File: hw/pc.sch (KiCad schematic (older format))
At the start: 8 parts, among them U601 74HC191, U602 74HC191, U603 74HC191, U604 74HC191, U605 74HC10, U606 74HC08, U607 74HC541, U608 74HC541

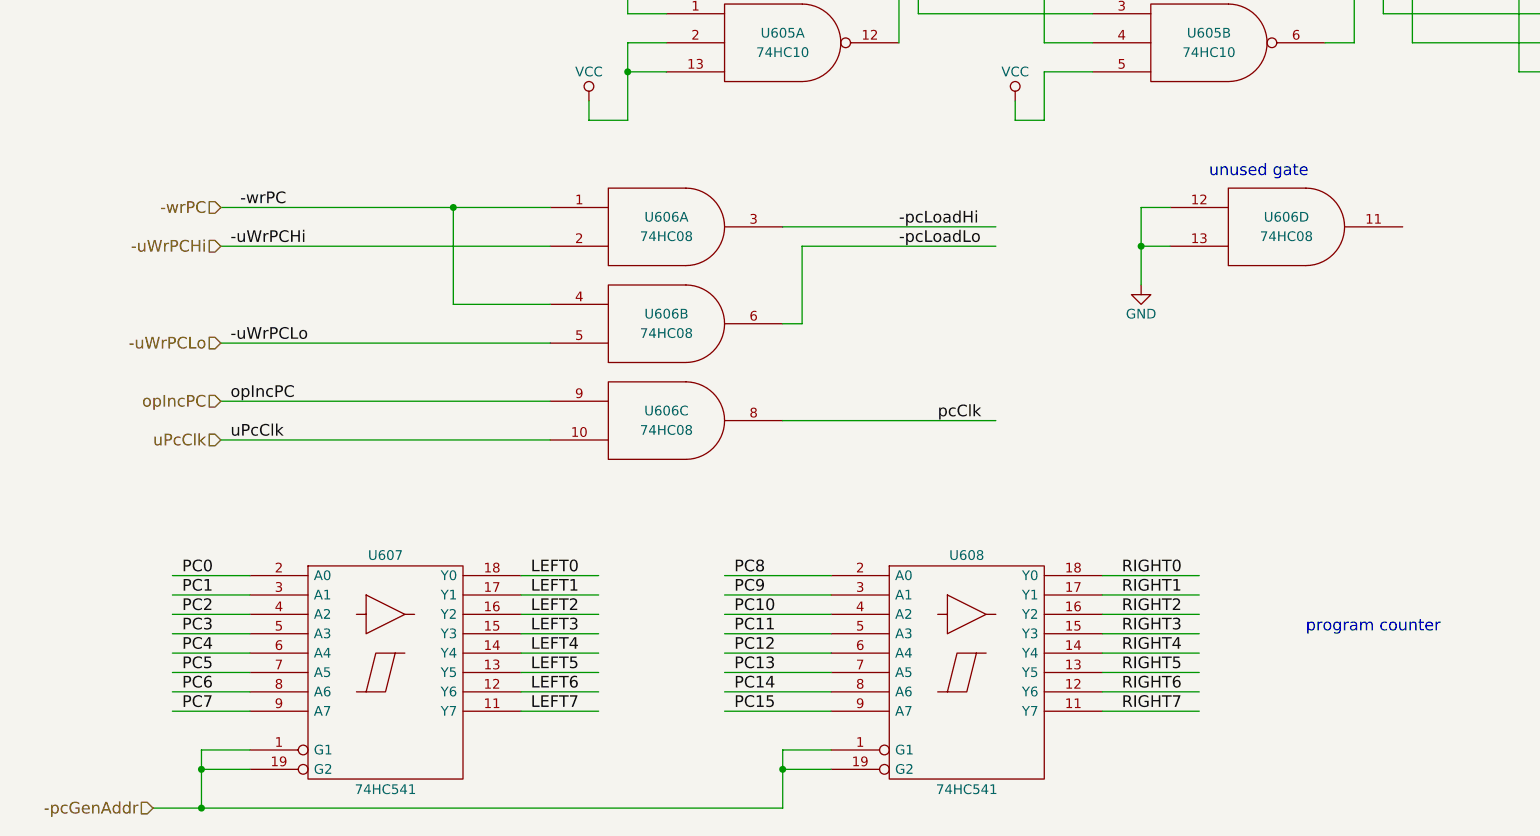
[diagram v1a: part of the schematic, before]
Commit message: use unused AND gate to allow 2 PC output enables
Both the opfetch logic and the microcode need to be
able to assert the contents of the PC onto the
left and right ALU input busses.
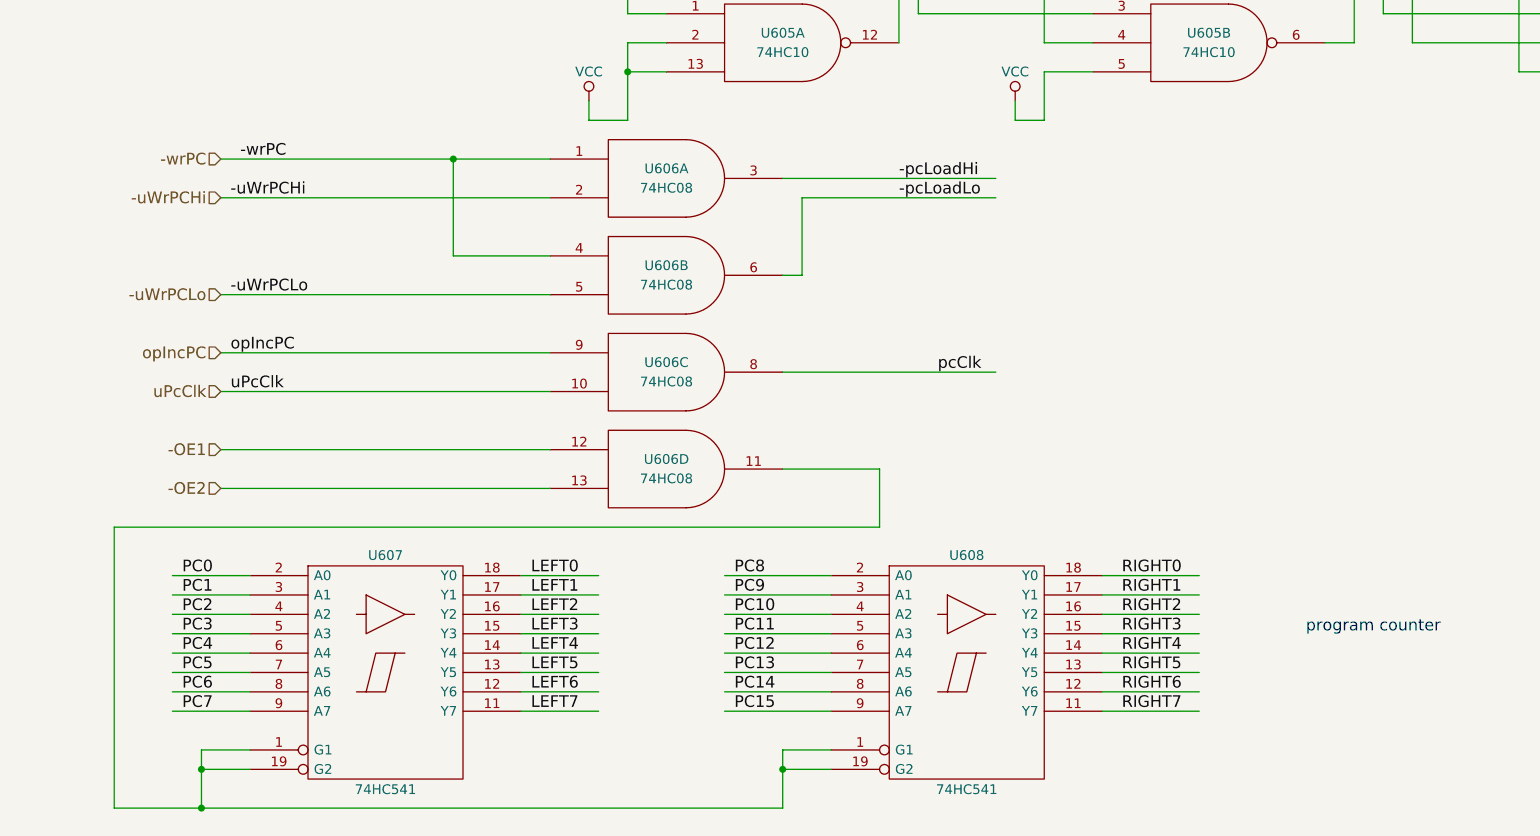
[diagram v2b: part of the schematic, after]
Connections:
- net labels added: -OE1, -OE2
- net labels removed: -pcGenAddr
- wire segments 184 -> 187
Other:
- note removed: "unused gate"
- moved on the sheet: U606A, U606B, U606C, U606D
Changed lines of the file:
@@
 Text Label 6200 7150 0    60   ~ 0
 RIGHT7
-Text HLabel 1200 7650 0    60   Input ~ 0
--pcGenAddr
+Text HLabel 1550 5800 0    60   Input ~ 0
+-OE1
 Text HLabel 1000 2050 0    60   Input ~ 0
 ALU0
@@
 Connection ~ 1450 7450
 Wire Wire Line
-	4450 7650 1200 7650
+	1000 7650 4450 7650
 Wire Wire Line
 	4700 7350 4450 7350
@@
 Connection ~ 6450 3150
 Wire Wire Line
-	1550 4550 3250 4550
-Text Label 1650 4550 0    60   ~ 0
+	1550 4300 3250 4300
+Text Label 1650 4300 0    60   ~ 0
 -wrPC
 Wire Wire Line
-	3250 5050 2750 5050
-Wire Wire Line
-	2750 5050 2750 4550
-Connection ~ 2750 4550
-Wire Wire Line
-	4450 4650 5550 4650
-Wire Wire Line
-	4450 5150 4550 5150
-Wire Wire Line
-	4550 5150 4550 4750
-Wire Wire Line
-	4550 4750 5550 4750
-Wire Wire Line
-	1550 5550 3250 5550
-Wire Wire Line
-	1550 5750 3250 5750
-Wire Wire Line
-	4450 5650 5550 5650
-Text Label 1600 5550 0    60   ~ 0
+	3250 4800 2750 4800
+Wire Wire Line
+	2750 4800 2750 4300
+Connection ~ 2750 4300
+Wire Wire Line
+	4450 4400 5550 4400
+Wire Wire Line
+	4450 4900 4550 4900
+Wire Wire Line
+	4550 4900 4550 4500
+Wire Wire Line
+	4550 4500 5550 4500
+Wire Wire Line
+	1550 5300 3250 5300
+Wire Wire Line
+	1550 5500 3250 5500
+Wire Wire Line
+	4450 5400 5550 5400
+Text Label 1600 5300 0    60   ~ 0
 opIncPC
 Wire Wire Line
-	3250 4750 1550 4750
-Wire Wire Line
-	3250 5250 1550 5250
-Text Label 1600 4750 0    60   ~ 0
+	3250 4500 1550 4500
+Wire Wire Line
+	3250 5000 1550 5000
+Text Label 1600 4500 0    60   ~ 0
 -uWrPCHi
-Text Label 1600 5250 0    60   ~ 0
+Text Label 1600 5000 0    60   ~ 0
 -uWrPCLo
-Text Label 1600 5750 0    60   ~ 0
+Text Label 1600 5500 0    60   ~ 0
 uPcClk
 Text Label 1450 700  0    60   ~ 0
@@
 Text Label 1450 1000 0    60   ~ 0
 -pcLoadLo
-Text HLabel 1550 4550 0    60   Input ~ 0
+Text HLabel 1550 4300 0    60   Input ~ 0
 -wrPC
-Text HLabel 1550 4750 0    60   Input ~ 0
+Text HLabel 1550 4500 0    60   Input ~ 0
 -uWrPCHi
-Text HLabel 1550 5250 0    60   Input ~ 0
+Text HLabel 1550 5000 0    60   Input ~ 0
 -uWrPCLo
-Text Label 5050 4650 0    60   ~ 0
+Text Label 5050 4400 0    60   ~ 0
 -pcLoadHi
-Text Label 5050 4750 0    60   ~ 0
+Text Label 5050 4500 0    60   ~ 0
 -pcLoadLo
 Text Label 1400 1500 0    60   ~ 0
 pcClk
-Text Label 5250 5650 0    60   ~ 0
+Text Label 5250 5400 0    60   ~ 0
 pcClk
-Text HLabel 1550 5550 0    60   Input ~ 0
+Text HLabel 1550 5300 0    60   Input ~ 0
 opIncPC
-Text HLabel 1550 5750 0    60   Input ~ 0
+Text HLabel 1550 5500 0    60   Input ~ 0
 uPcClk
 $Comp
 L 74LS08 U606
 U 1 1 5943D28D
-P 3850 4650
-F 0 "U606" H 3850 4700 50  0000 C CNN
-F 1 "74HC08" H 3850 4600 50  0000 C CNN
-F 2 "" H 3850 4650 50  0001 C CNN
-F 3 "" H 3850 4650 50  0001 C CNN
-	1    3850 4650
+P 3850 4400
+F 0 "U606" H 3850 4450 50  0000 C CNN
+F 1 "74HC08" H 3850 4350 50  0000 C CNN
+F 2 "" H 3850 4400 50  0001 C CNN
+F 3 "" H 3850 4400 50  0001 C CNN
+	1    3850 4400
 	1    0    0    -1
 $EndComp
@@
 L 74LS08 U606
 U 2 1 5943D2BC
-P 3850 5150
-F 0 "U606" H 3850 5200 50  0000 C CNN
-F 1 "74HC08" H 3850 5100 50  0000 C CNN
-F 2 "" H 3850 5150 50  0001 C CNN
-F 3 "" H 3850 5150 50  0001 C CNN
-	2    3850 5150
+P 3850 4900
+F 0 "U606" H 3850 4950 50  0000 C CNN
+F 1 "74HC08" H 3850 4850 50  0000 C CNN
+F 2 "" H 3850 4900 50  0001 C CNN
+F 3 "" H 3850 4900 50  0001 C CNN
+	2    3850 4900
 	1    0    0    -1
 $EndComp
@@
 L 74LS08 U606
 U 3 1 5943D307
-P 3850 5650
-F 0 "U606" H 3850 5700 50  0000 C CNN
-F 1 "74HC08" H 3850 5600 50  0000 C CNN
-F 2 "" H 3850 5650 50  0001 C CNN
-F 3 "" H 3850 5650 50  0001 C CNN
-	3    3850 5650
+P 3850 5400
+F 0 "U606" H 3850 5450 50  0000 C CNN
+F 1 "74HC08" H 3850 5350 50  0000 C CNN
+F 2 "" H 3850 5400 50  0001 C CNN
+F 3 "" H 3850 5400 50  0001 C CNN
+	3    3850 5400
 	1    0    0    -1
 $EndComp
@@
 L 74LS08 U606
 U 4 1 5943D865
-P 7050 4650
-F 0 "U606" H 7050 4700 50  0000 C CNN
-F 1 "74HC08" H 7050 4600 50  0000 C CNN
-F 2 "" H 7050 4650 50  0001 C CNN
-F 3 "" H 7050 4650 50  0001 C CNN
-	4    7050 4650
-	1    0    0    -1
-$EndComp
-Wire Wire Line
-	6450 4550 6300 4550
-Wire Wire Line
-	6300 4550 6300 4950
-Wire Wire Line
-	6450 4750 6300 4750
-Connection ~ 6300 4750
-$Comp
-L GND #PWR?
-U 1 1 5943DB03
-P 6300 4950
-F 0 "#PWR?" H 6300 4700 50  0001 C CNN
-F 1 "GND" H 6300 4800 50  0000 C CNN
-F 2 "" H 6300 4950 50  0001 C CNN
-F 3 "" H 6300 4950 50  0001 C CNN
-	1    6300 4950
-	1    0    0    -1
-$EndComp
-Text Notes 6650 4400 0    60   ~ 0
-unused gate
+P 3850 5900
+F 0 "U606" H 3850 5950 50  0000 C CNN
+F 1 "74HC08" H 3850 5850 50  0000 C CNN
+F 2 "" H 3850 5900 50  0001 C CNN
+F 3 "" H 3850 5900 50  0001 C CNN
+	4    3850 5900
+	1    0    0    -1
+$EndComp
+Wire Wire Line
+	3250 5800 1550 5800
+Wire Wire Line
+	3250 6000 1550 6000
+Text HLabel 1550 6000 0    60   Input ~ 0
+-OE2
+Wire Wire Line
+	4450 5900 4950 5900
+Wire Wire Line
+	4950 5900 4950 6200
+Wire Wire Line
+	4950 6200 1000 6200
+Wire Wire Line
+	1000 6200 1000 7650
 $EndSCHEMATC

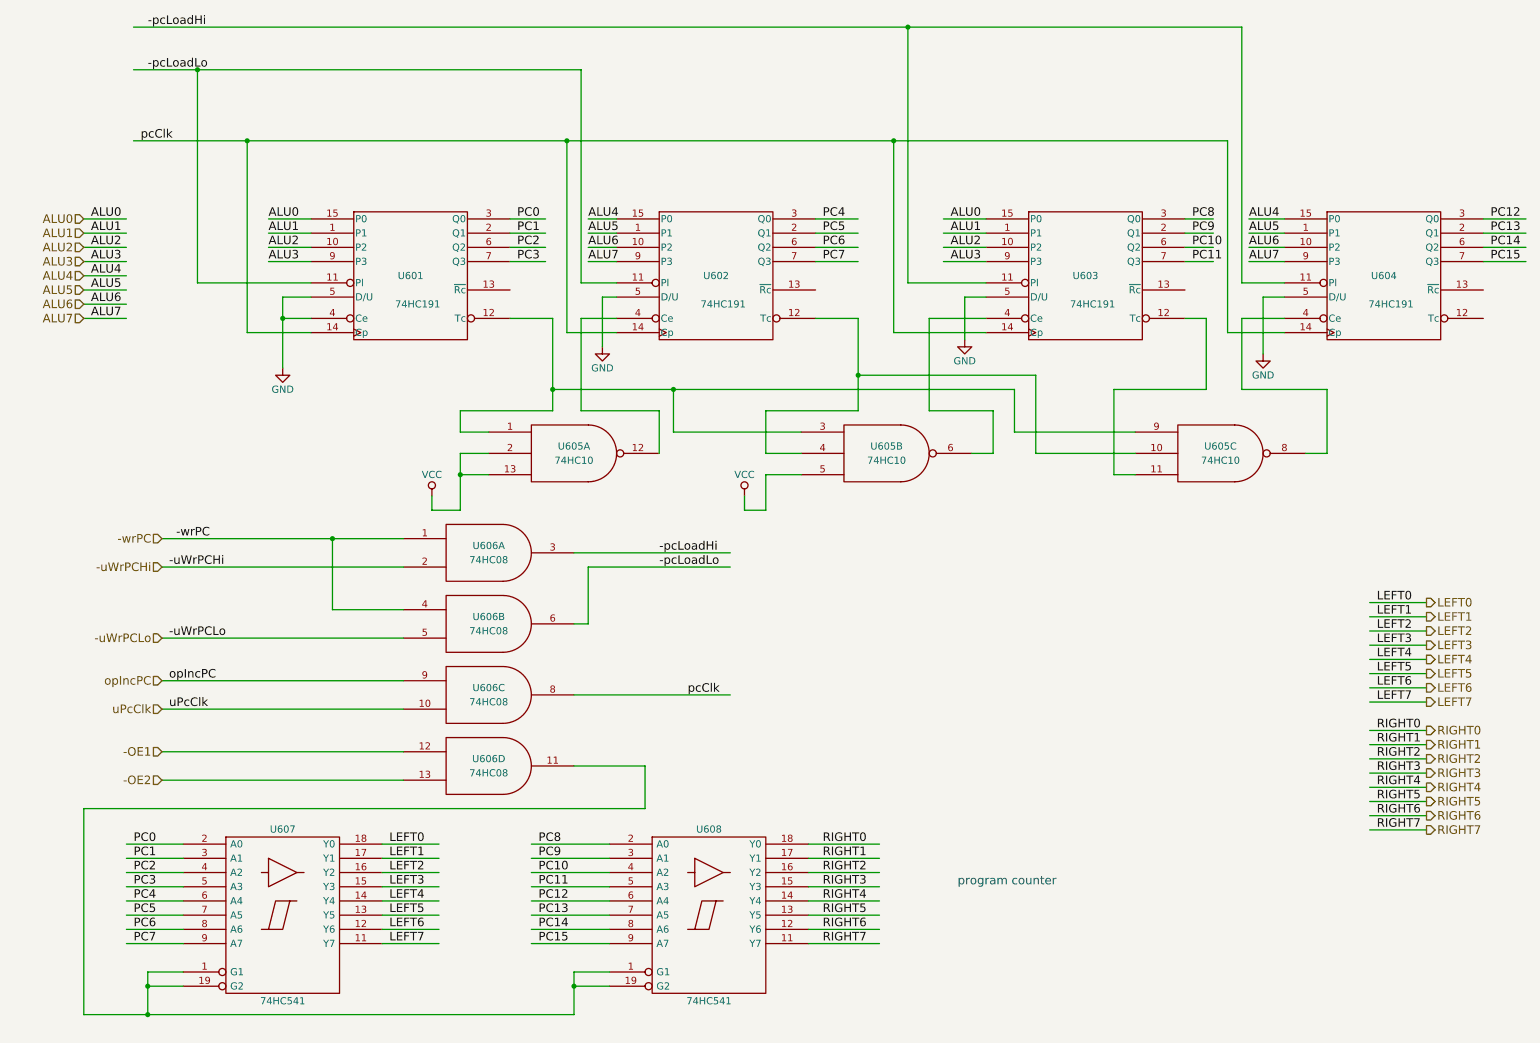
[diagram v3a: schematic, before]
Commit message: simplified control of output to left/right busses
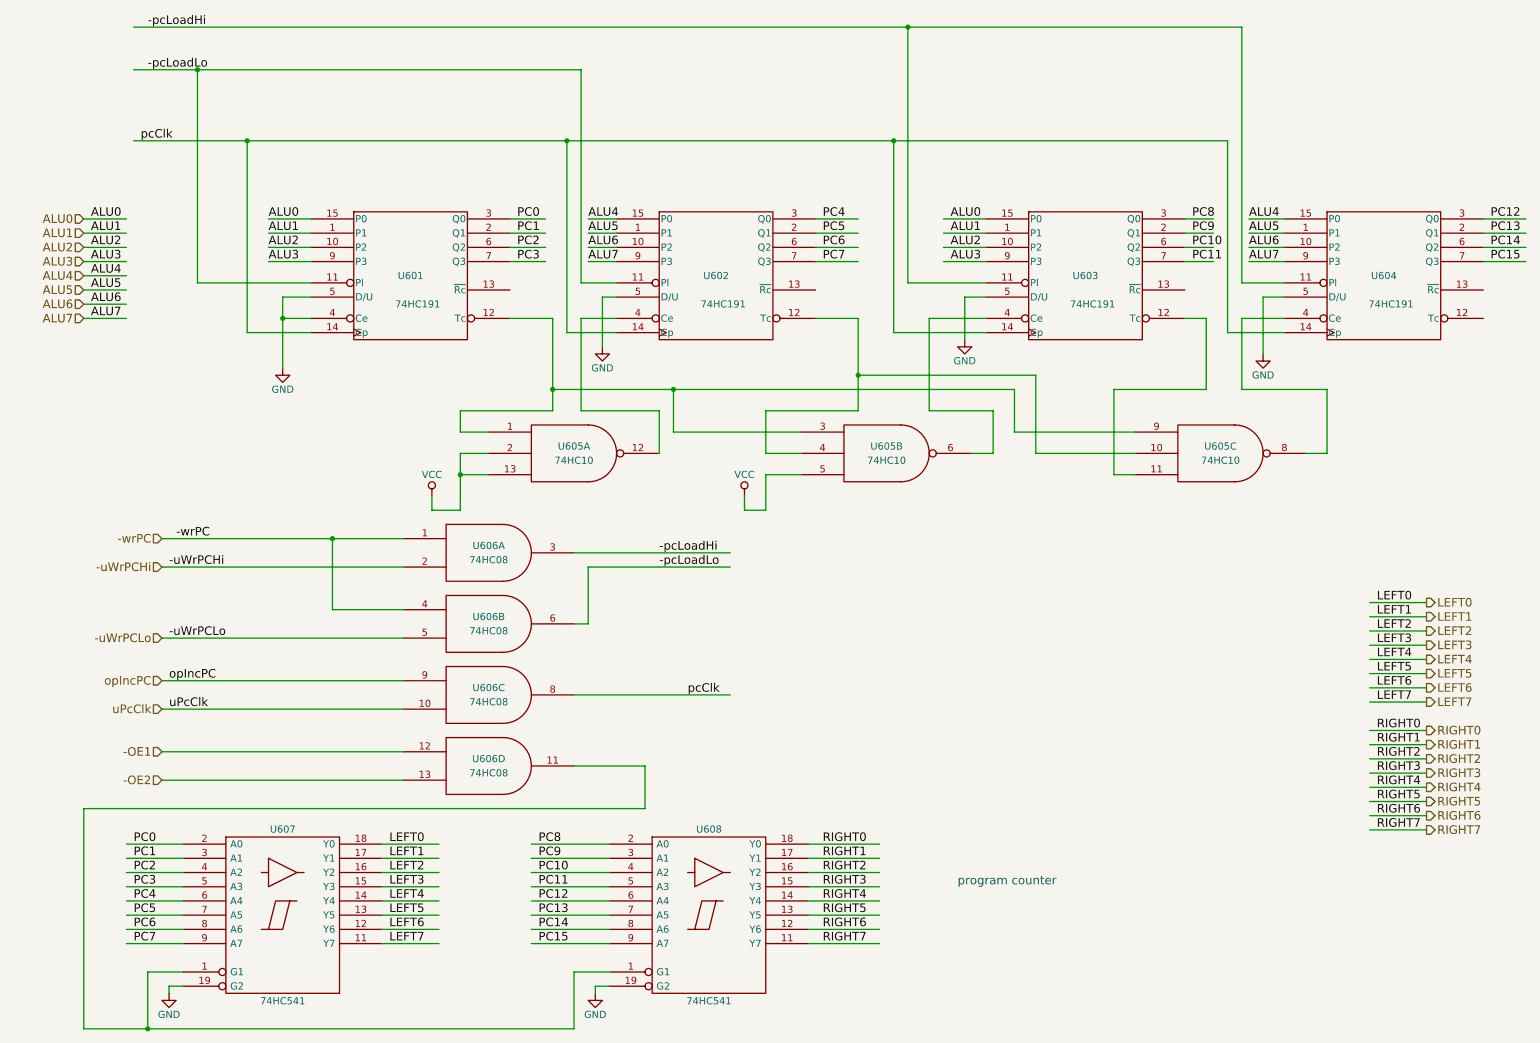
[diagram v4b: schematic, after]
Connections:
- wire segments 187 -> 201
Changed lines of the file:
@@
 	2600 2600 2400 2600
 Wire Wire Line
-	2400 2600 2400 3100
+	2400 2600 2400 2750
+Wire Wire Line
+	2400 2750 2400 3100
 Wire Wire Line
 	4750 2600 4650 2600
@@
 	9050 2850 9050 1500
 Wire Wire Line
-	9050 1500 1350 1500
+	9050 1500 6700 1500
+Wire Wire Line
+	6700 1500 4400 1500
+Wire Wire Line
+	4400 1500 2150 1500
+Wire Wire Line
+	2150 1500 1350 1500
 Wire Wire Line
 	7350 2850 6700 2850
@@
 	1800 2500 1800 1000
 Wire Wire Line
-	1350 1000 4500 1000
+	1350 1000 1800 1000
+Wire Wire Line
+	1800 1000 4500 1000
 Wire Wire Line
 	4750 2500 4500 2500
@@
 	6800 2500 6800 700
 Wire Wire Line
-	1350 700  9150 700
+	1350 700  6800 700
+Wire Wire Line
+	6800 700  9150 700
 Wire Wire Line
 	9450 2500 9150 2500
@@
 	1700 7350 1450 7350
 Wire Wire Line
-	1450 7350 1450 7650
-Wire Wire Line
-	1700 7450 1450 7450
-Connection ~ 1450 7450
-Wire Wire Line
-	1000 7650 4450 7650
+	1450 7350 1450 7750
+Wire Wire Line
+	1000 7750 1450 7750
+Wire Wire Line
+	1450 7750 4450 7750
 Wire Wire Line
 	4700 7350 4450 7350
 Wire Wire Line
-	4450 7350 4450 7650
-Connection ~ 1450 7650
-Wire Wire Line
-	4700 7450 4450 7450
-Connection ~ 4450 7450
+	4450 7350 4450 7750
+Connection ~ 1450 7750
 Wire Wire Line
 	8750 2350 8950 2350
@@
 Connection ~ 2400 2750
 Wire Wire Line
-	4300 2750 4300 3400
+	4300 2750 4300 3250
+Wire Wire Line
+	4300 3250 4300 3400
 Wire Wire Line
 	4300 3400 3650 3400
@@
 	4500 3400 4500 2750
 Wire Wire Line
-	6450 2750 6450 3400
+	6450 2750 6450 3150
+Wire Wire Line
+	6450 3150 6450 3400
 Wire Wire Line
 	6450 3400 5800 3400
@@
 	7550 3550 7550 3250
 Wire Wire Line
-	7550 3250 4300 3250
+	7550 3250 5150 3250
+Wire Wire Line
+	5150 3250 4300 3250
 Wire Wire Line
 	8900 2750 8900 3250
@@
 	3850 3850 3650 3850
 Wire Wire Line
-	3650 3700 3650 4100
+	3650 3700 3650 3850
+Wire Wire Line
+	3650 3850 3650 4100
 Wire Wire Line
 	3650 4100 3450 4100
@@
 Connection ~ 6450 3150
 Wire Wire Line
-	1550 4300 3250 4300
+	1550 4300 2750 4300
+Wire Wire Line
+	2750 4300 3250 4300
 Text Label 1650 4300 0    60   ~ 0
 -wrPC
@@
 	4950 6200 1000 6200
 Wire Wire Line
-	1000 6200 1000 7650
+	1000 6200 1000 7750
+Wire Wire Line
+	1700 7450 1600 7450
+Wire Wire Line
+	1600 7450 1600 7500
+$Comp
+L GND #PWR?
+U 1 1 59621AEE
+P 1600 7500
+F 0 "#PWR?" H 1600 7250 50  0001 C CNN
+F 1 "GND" H 1600 7350 50  0000 C CNN
+F 2 "" H 1600 7500 50  0001 C CNN
+F 3 "" H 1600 7500 50  0001 C CNN
+	1    1600 7500
+	1    0    0    -1
+$EndComp
+Wire Wire Line
+	4700 7450 4600 7450
+Wire Wire Line
+	4600 7450 4600 7500
+$Comp
+L GND #PWR?
+U 1 1 59621B43
+P 4600 7500
+F 0 "#PWR?" H 4600 7250 50  0001 C CNN
+F 1 "GND" H 4600 7350 50  0000 C CNN
+F 2 "" H 4600 7500 50  0001 C CNN
+F 3 "" H 4600 7500 50  0001 C CNN
+	1    4600 7500
+	1    0    0    -1
+$EndComp
 $EndSCHEMATC

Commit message: account for opfetch for -uExtR and -uRwMem
-uExtR should be asserted whenever -opReadMem is asserted,
and -uRwMem should be asserted whenever -opfetch is asserted.

Did this without additional chips, at the cost of requiring
74HCT10 rather than 74HCT20 in the conditional branch logic.
(Will have to buy these, but I've seen them on ebay.)

Also renumbered some of the chips in the ucode2 module
so that the numbering reflects the actual number of chips
(16).

Will need to carefully double check this to make sure it's
correct.
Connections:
- wire segments 201 -> 189
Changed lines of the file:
@@
 	2600 2600 2400 2600
 Wire Wire Line
-	2400 2600 2400 2750
-Wire Wire Line
-	2400 2750 2400 3100
+	2400 2600 2400 3100
 Wire Wire Line
 	4750 2600 4650 2600
@@
 	9450 2850 9050 2850
 Wire Wire Line
-	9050 2850 9050 1500
-Wire Wire Line
-	9050 1500 6700 1500
-Wire Wire Line
-	6700 1500 4400 1500
-Wire Wire Line
-	4400 1500 2150 1500
-Wire Wire Line
-	2150 1500 1350 1500
+	9050 1500 9050 2850
+Wire Wire Line
+	1350 1500 9050 1500
 Wire Wire Line
 	7350 2850 6700 2850
@@
 	1800 2500 1800 1000
 Wire Wire Line
-	1350 1000 1800 1000
-Wire Wire Line
-	1800 1000 4500 1000
+	1350 1000 4500 1000
 Wire Wire Line
 	4750 2500 4500 2500
@@
 	6800 2500 6800 700
 Wire Wire Line
-	1350 700  6800 700
-Wire Wire Line
-	6800 700  9150 700
+	1350 700  9150 700
 Wire Wire Line
 	9450 2500 9150 2500
@@
 	1450 7350 1450 7750
 Wire Wire Line
-	1000 7750 1450 7750
-Wire Wire Line
-	1450 7750 4450 7750
+	1000 7750 4450 7750
 Wire Wire Line
 	4700 7350 4450 7350
@@
 Connection ~ 2400 2750
 Wire Wire Line
-	4300 2750 4300 3250
-Wire Wire Line
-	4300 3250 4300 3400
+	4300 2750 4300 3400
 Wire Wire Line
 	4300 3400 3650 3400
@@
 	4500 3400 4500 2750
 Wire Wire Line
-	6450 2750 6450 3150
-Wire Wire Line
-	6450 3150 6450 3400
+	6450 2750 6450 3400
 Wire Wire Line
 	6450 3400 5800 3400
@@
 	8400 3550 7550 3550
 Wire Wire Line
-	7550 3550 7550 3250
-Wire Wire Line
-	7550 3250 5150 3250
-Wire Wire Line
-	5150 3250 4300 3250
+	7550 3250 7550 3550
+Wire Wire Line
+	4300 3250 7550 3250
 Wire Wire Line
 	8900 2750 8900 3250
@@
 	3850 3850 3650 3850
 Wire Wire Line
-	3650 3700 3650 3850
-Wire Wire Line
-	3650 3850 3650 4100
+	3650 3700 3650 4100
 Wire Wire Line
 	3650 4100 3450 4100
@@
 Connection ~ 6450 3150
 Wire Wire Line
-	1550 4300 2750 4300
-Wire Wire Line
-	2750 4300 3250 4300
+	1550 4300 3250 4300
 Text Label 1650 4300 0    60   ~ 0
 -wrPC
